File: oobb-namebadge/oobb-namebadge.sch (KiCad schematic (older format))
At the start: 4 parts, among them J1 Conn_02x03_Row_Letter_First, J2 Conn_02x03_Row_Letter_First, J3 Conn_02x03_Row_Letter_First, J4 Conn_02x03_Row_Letter_First

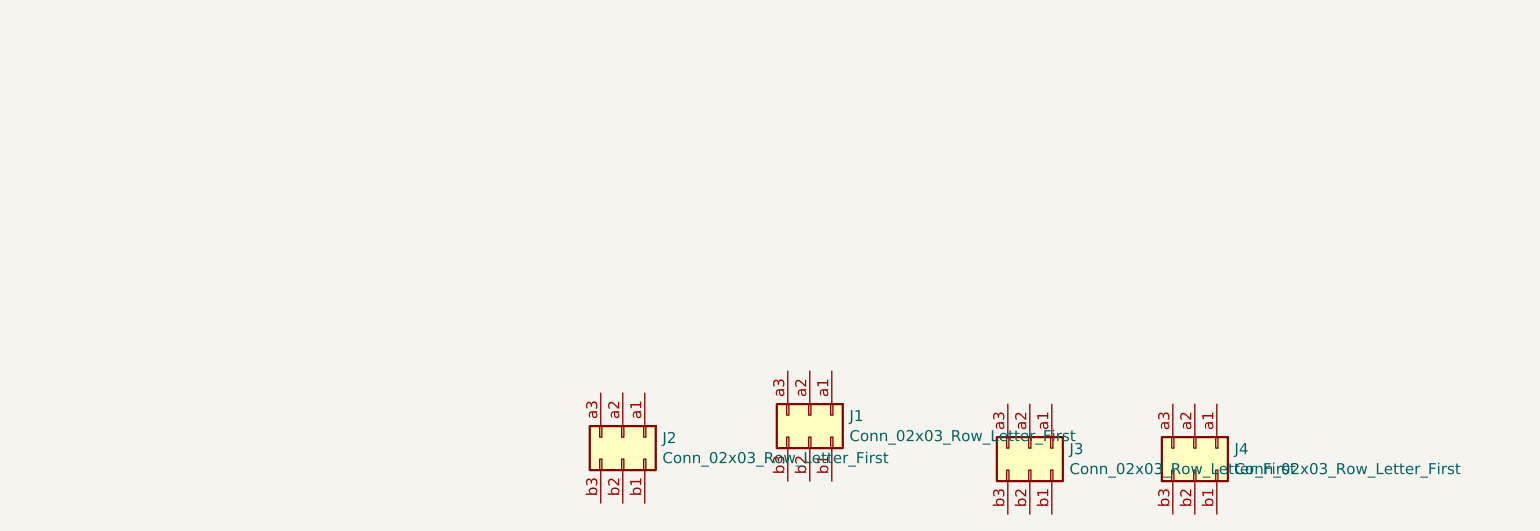
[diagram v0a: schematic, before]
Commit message: needs lipo charger
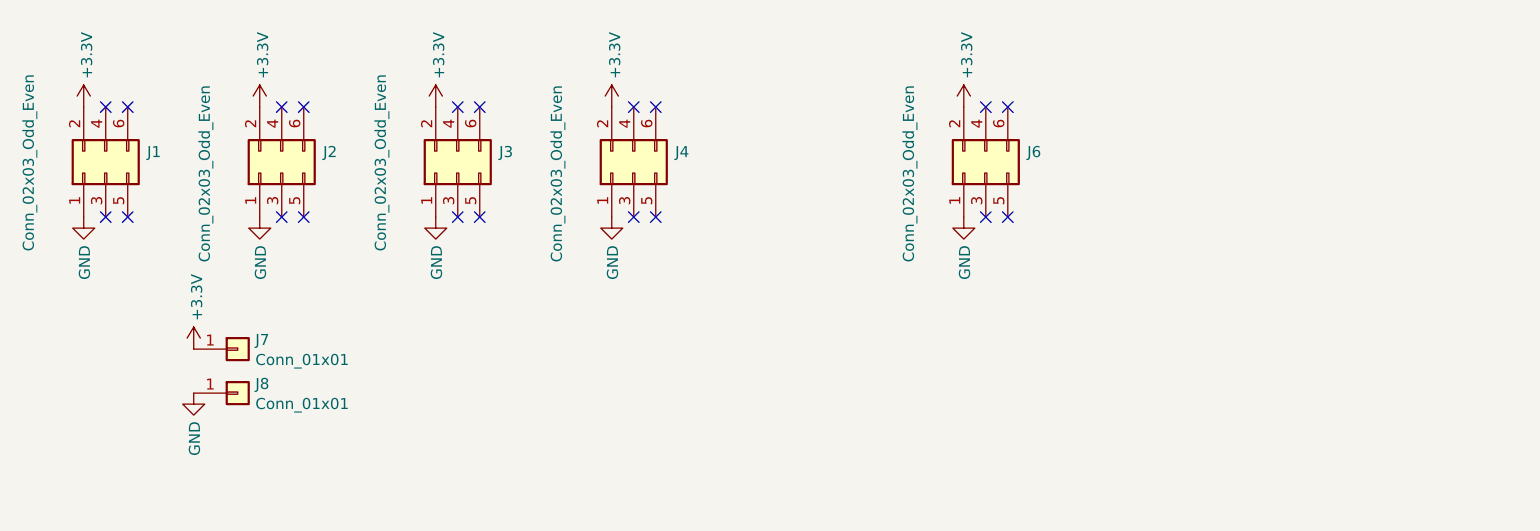
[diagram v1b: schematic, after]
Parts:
- removed J1, J2, J3, J4: Conn_02x03_Row_Letter_First, Pin_Headers:Pin_Header_Straight_2x03_Pitch2.54mm, symbol Conn_02x03_Row_Letter_First
- added J1, J2, J3, J4, J6: Conn_02x03_Odd_Even, oobb:Pin_Header_Straight_2x03_Pitch2.54mm, symbol Conn_02x03_Odd_Even
- added J7, J8: Conn_01x01, Connectors_TestPoints:Test_Point_Pad_d1.5mm, symbol Conn_01x01
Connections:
- new net +3V3: J1.2 (Pin_2), J2.2 (Pin_2), J3.2 (Pin_2), J4.2 (Pin_2), J6.2 (Pin_2), J7.1 (Pin_1)
- new net GND: J1.1 (Pin_1), J2.1 (Pin_1), J3.1 (Pin_1), J4.1 (Pin_1), J6.1 (Pin_1), J8.1 (Pin_1)
- no-connect marks 0 -> 20

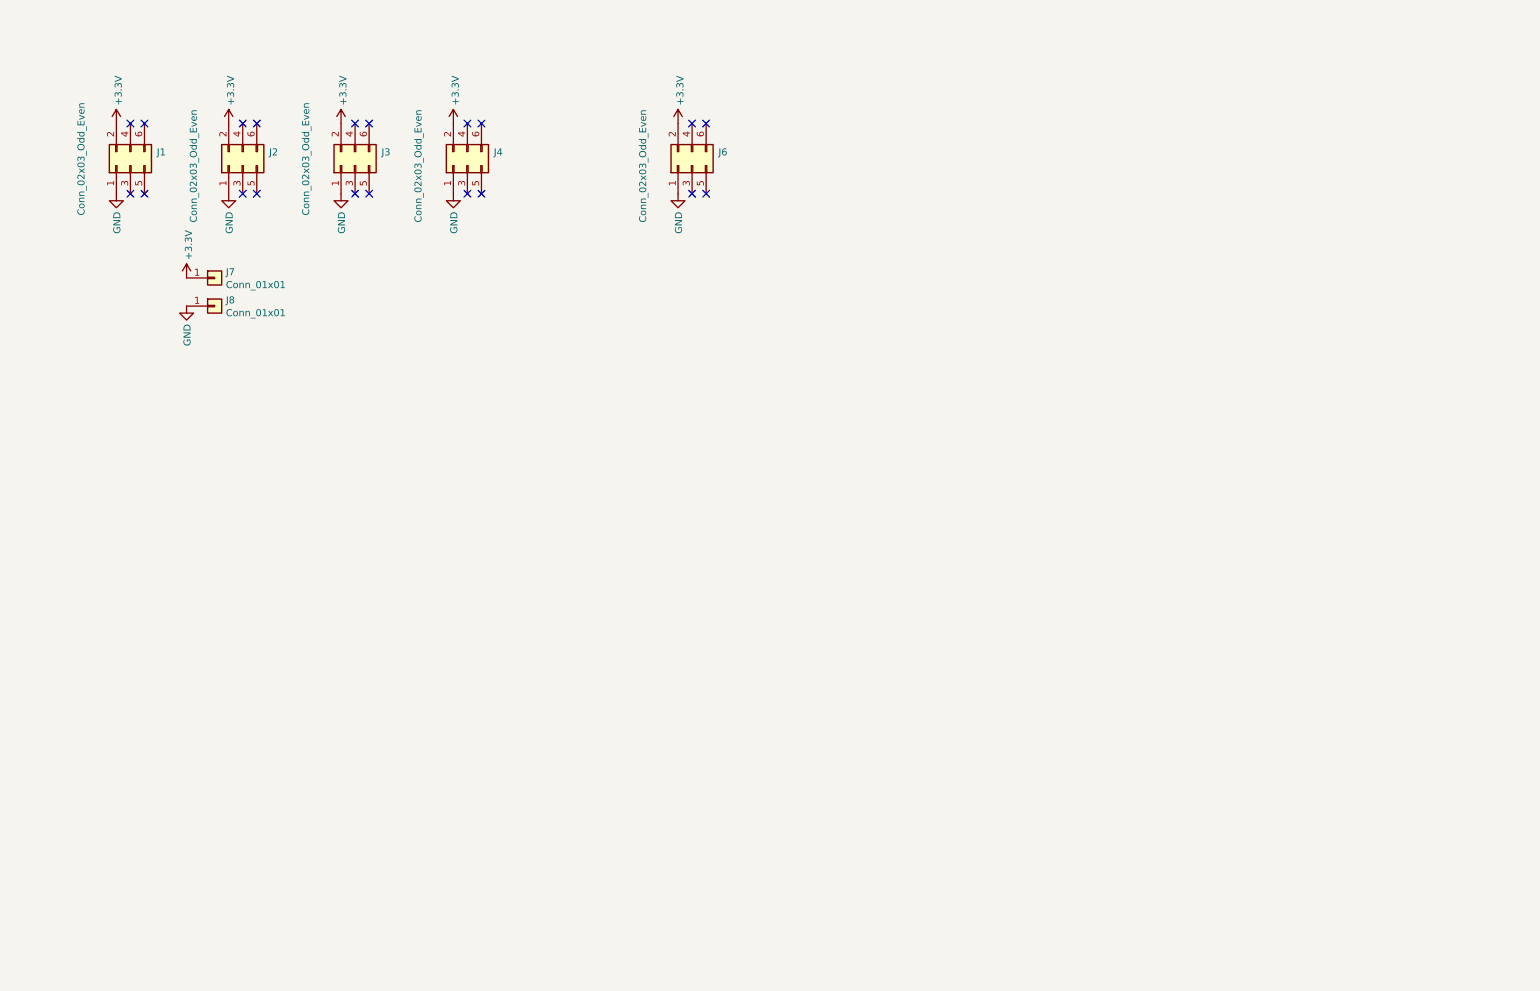
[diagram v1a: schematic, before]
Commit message: added icebreaker, ldo, switch and boost board
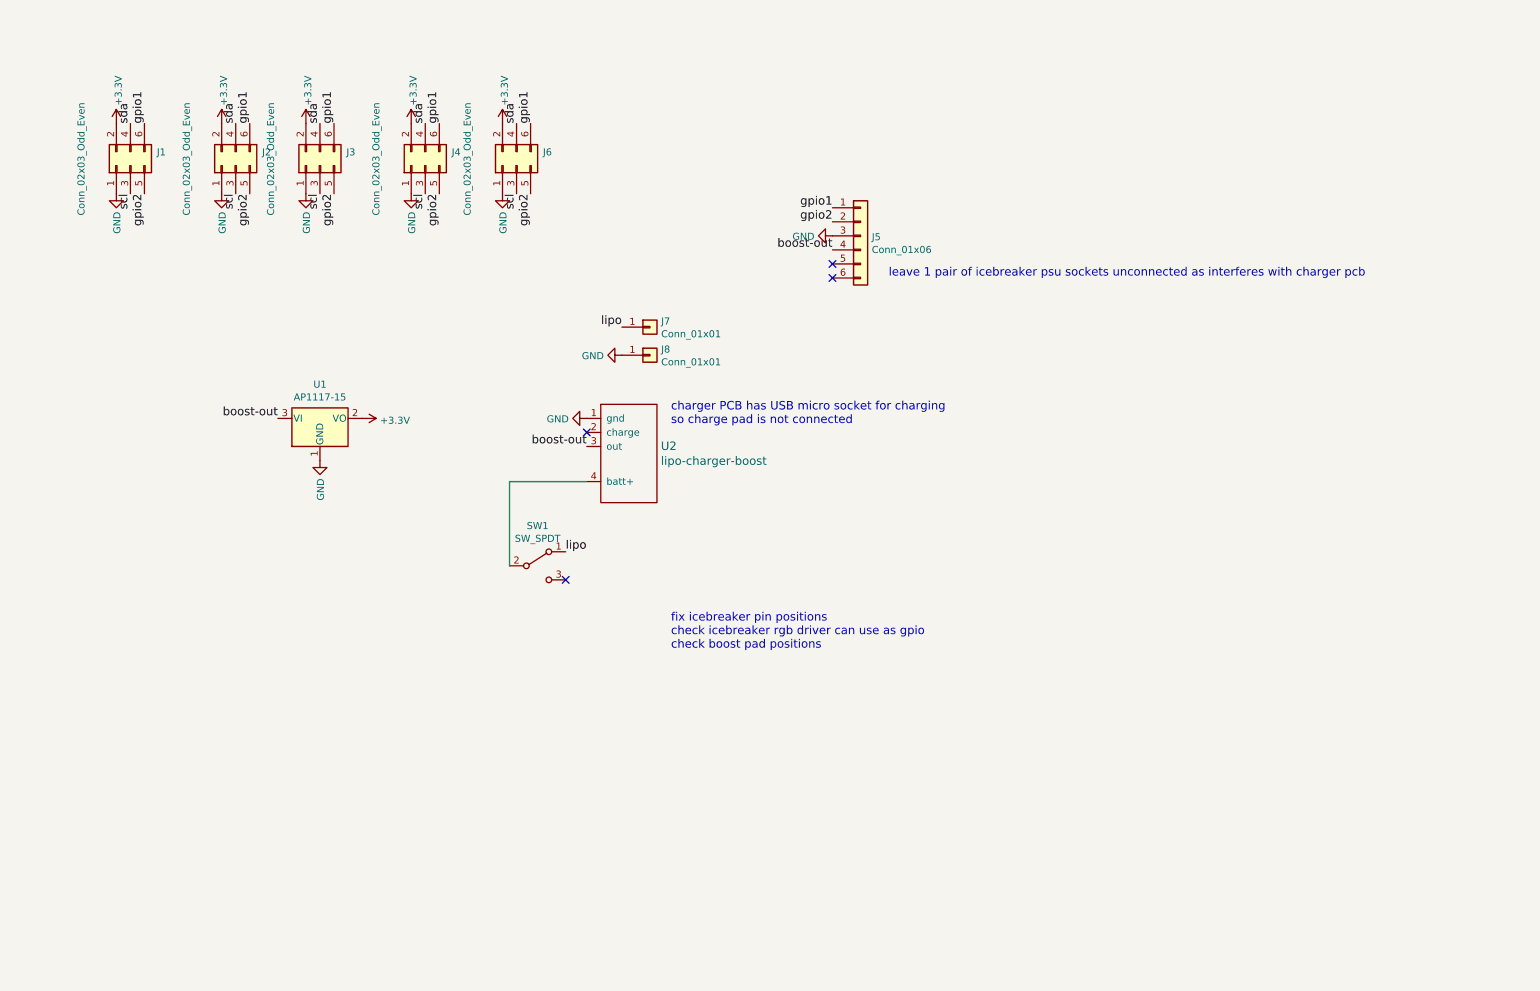
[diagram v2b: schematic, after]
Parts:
- added J5: Conn_01x06, oobb:icebreaker, symbol Conn_01x06
- added SW1: SW_SPDT, Buttons_Switches_SMD:SW_SPDT_CK-JS102011SAQN, symbol SW_SPDT
- added U1: AP1117-15, TO_SOT_Packages_SMD:SOT-223, symbol AP1117-15
- added U2: lipo-charger-boost, oobb:lipo-charger-boost, symbol lipo-charger-boost
- J6: MOQ (none) -> Value; leadtime (none) -> Value; supplier (none) -> Value; supplier PN (none) -> Value
- J7, J8: footprint Connectors_TestPoints:Test_Point_Pad_d1.5mm -> Measurement_Points:Measurement_Point_Square-SMD-Pad_Big
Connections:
- net +3V3: now also U1.2 (VO); no longer J7.1 (Pin_1)
- net GND: now also J5.3 (Pin_3), U1.1 (GND), U2.1 (gnd)
- net scl: now reaches J1.3 (Pin_3)
- net scl: now also J2.3 (Pin_3), J3.3 (Pin_3), J4.3 (Pin_3), J6.3 (Pin_3)
- net sda: now reaches J1.4 (Pin_4)
- net sda: now also J2.4 (Pin_4), J3.4 (Pin_4), J4.4 (Pin_4), J6.4 (Pin_4)
- net gpio2: now reaches J1.5 (Pin_5)
- net gpio2: now also J2.5 (Pin_5), J3.5 (Pin_5), J4.5 (Pin_5), J6.5 (Pin_5), J5.2 (Pin_2)
- net gpio1: now reaches J1.6 (Pin_6)
- net gpio1: now also J2.6 (Pin_6), J3.6 (Pin_6), J4.6 (Pin_6), J6.6 (Pin_6), J5.1 (Pin_1)
- new net: SW1.2 (B), U2.4 (batt+)
- new net boost-out: J5.4 (Pin_4), U1.3 (VI), U2.3 (out)
- new net lipo: J7.1 (Pin_1), SW1.1 (A)
- no-connect marks 20 -> 4
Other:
- note added: "charger PCB has USB micro socket for charging\nso charge pad is not connected"
- note added: "fix icebreaker pin positions\ncheck icebreaker rgb driver can use as gpio\ncheck boost pad positions\n"
- note added: "leave 1 pair of icebreaker psu sockets unconnected as interferes with charger pcb"
- moved on the sheet: J7, J8

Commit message: ready to fab
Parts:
- added R1, R2: 10k, Resistors_SMD:R_0805_HandSoldering, symbol R
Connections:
- net +3V3: now also R1.2, R2.2
- net gpio1: now also R1.1
- net gpio2: now also R2.1
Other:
- note added: "\n"
- note added: "pullups for LED driver output of icebreaker to control GPIOs for SAOs\n"
- note removed: "fix icebreaker pin positions\ncheck icebreaker rgb driver can use as gpio\ncheck boost pad positions\n"
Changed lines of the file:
@@
 charger PCB has USB micro socket for charging\nso charge pad is not connected
 Text Notes 6100 5200 0    60   ~ 0
-fix icebreaker pin positions\ncheck icebreaker rgb driver can use as gpio\ncheck boost pad positions\n
+\n
 Text Notes 7650 2550 0    60   ~ 0
 leave 1 pair of icebreaker psu sockets unconnected as interferes with charger pcb
+$Comp
+L R R1
+U 1 1 5D9F3122
+P 6600 1450
+F 0 "R1" H 6670 1496 50  0000 L CNN
+F 1 "10k" H 6670 1405 50  0000 L CNN
+F 2 "Resistors_SMD:R_0805_HandSoldering" V 6530 1450 50  0001 C CNN
+F 3 "" H 6600 1450 50  0001 C CNN
+F 4 "Value" H 6600 1450 60  0001 C CNN "supplier"
+F 5 "Value" H 6600 1450 60  0001 C CNN "supplier PN"
+F 6 "Value" H 6600 1450 60  0001 C CNN "MOQ"
+F 7 "Value" H 6600 1450 60  0001 C CNN "leadtime"
+	1    6600 1450
+	1    0    0    -1
+$EndComp
+$Comp
+L R R2
+U 1 1 5D9F317E
+P 6800 1450
+F 0 "R2" H 6870 1496 50  0000 L CNN
+F 1 "10k" H 6870 1405 50  0000 L CNN
+F 2 "Resistors_SMD:R_0805_HandSoldering" V 6730 1450 50  0001 C CNN
+F 3 "" H 6800 1450 50  0001 C CNN
+F 4 "Value" H 6800 1450 60  0001 C CNN "supplier"
+F 5 "Value" H 6800 1450 60  0001 C CNN "supplier PN"
+F 6 "Value" H 6800 1450 60  0001 C CNN "MOQ"
+F 7 "Value" H 6800 1450 60  0001 C CNN "leadtime"
+	1    6800 1450
+	1    0    0    -1
+$EndComp
+Text Label 6600 1300 1    60   ~ 0
+gpio1
+Text Label 6800 1300 1    60   ~ 0
+gpio2
+$Comp
+L +3.3V #PWR014
+U 1 1 5D9F3332
+P 6600 1600
+F 0 "#PWR014" H 6600 1450 50  0001 C CNN
+F 1 "+3.3V" V 6615 1728 50  0000 L CNN
+F 2 "" H 6600 1600 50  0001 C CNN
+F 3 "" H 6600 1600 50  0001 C CNN
+	1    6600 1600
+	-1   0    0    1
+$EndComp
+$Comp
+L +3.3V #PWR017
+U 1 1 5D9F3398
+P 6800 1600
+F 0 "#PWR017" H 6800 1450 50  0001 C CNN
+F 1 "+3.3V" V 6815 1728 50  0000 L CNN
+F 2 "" H 6800 1600 50  0001 C CNN
+F 3 "" H 6800 1600 50  0001 C CNN
+	1    6800 1600
+	-1   0    0    1
+$EndComp
+Text Notes 6350 950  0    60   ~ 0
+pullups for LED driver output of icebreaker to control GPIOs for SAOs\n
 $EndSCHEMATC
